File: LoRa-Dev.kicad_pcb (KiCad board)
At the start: 2 copper layers, 14 parts, among them J2 Barrel_Jack_MountingPin, U1 RPi Pico, U2 LT1963AEQ

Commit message: board layout
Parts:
- added C3: 47uF, Capacitor_SMD:CP_Elec_6.3x5.8, F.Cu at (126.5, 59.0)
- added C4: 0.1uF, Capacitor_SMD:C_0603_1608Metric, F.Cu at (128.0, 65.5)
- added J1: Conn_Coaxial_Small, Connector_Coaxial:U.FL_Hirose_U.FL-R-SMT-1_Vertical, F.Cu at (114.5, 60.0)
- added R9: R_Small, Resistor_SMD:R_0603_1608Metric, F.Cu at (126.7, 53.5)
- added U3: LoRa126XF30, LoRa-Dev:LoRa126XF30, F.Cu at (119.0, 82.5)
- moved U1 74.5 mm to (134.5, 41.1), turned to -90 degrees
- moved C1 2.50 mm to (143.0, 68.5)
- moved C2 2.00 mm to (152.0, 60.5)
- moved F1 2.00 mm to (159.0, 63.0)
- moved R7 2.00 mm to (156.0, 58.5)
- moved R8 2.00 mm to (159.0, 58.5)
- moved U2 2.00 mm to (138.6, 61.0)
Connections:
- net Net-(J2-Pad1) renamed /12V
- J2 pad MP: unconnected-(J2-MountPin-PadMP) -> GND
- U1 pad 26: unconnected-(U1-GP20-Pad26) -> /DIO3
- U1 pad 27: unconnected-(U1-GP21-Pad27) -> /DIO1
- U1 pad 29: unconnected-(U1-GP22-Pad29) -> /RESETn
- U1 pad 31: unconnected-(U1-GP26-Pad31) -> /BUSY
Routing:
- net /SPI_CSn: track 0.00 -> 60.4 mm, vias 0 -> 1
- net /SPI_SCK: track 0.00 -> 52.0 mm, vias 0 -> 1
- net RF_VDD: track 0.00 -> 49.8 mm, vias 0 -> 4
- net /BUSY: track 0.00 -> 45.5 mm, vias 0 -> 1
- net /DIO1: track 0.00 -> 45.4 mm, vias 0 -> 1
- net /SPI_MOSI: track 0.00 -> 44.7 mm, vias 0 -> 1
- net /SPI_MISO: track 0.00 -> 44.2 mm, vias 0 -> 1
- net /DIO3: track 0.00 -> 39.5 mm, vias 0 -> 1
- net /RESETn: track 0.00 -> 36.5 mm, vias 0 -> 1
- net /ANT: track 0.00 -> 10.0 mm
- net GND: track 21.3 -> 20.8 mm, vias 0 -> 32
- added copper zone on F.Cu, net /RF_GND
- added copper zone on In1.Cu, net /RF_GND
- added copper zone on B.Cu, net GND
- added copper zone on F.Cu, net GND
- added copper zone on In1.Cu, net GND
- added copper zone on In2.Cu, net GND
- added copper zone on F.Cu, net RF_VDD
- added copper zone on In2.Cu, net RF_VDD
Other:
- board outline added: 56 x 71 mm
- copper layers 2 -> 4

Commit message: Update silkscreen
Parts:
- R7: value 1k5 -> 4k7
- R8: value 4k7 -> 1k5
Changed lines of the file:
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@@
 		(tags "resistor")
 		(property "Reference" "R5"
-			(at 0 -2.62 0)
+			(at 4 0 90)
 			(layer "F.SilkS")
 			(effects
@@
 		(tags "resistor")
 		(property "Reference" "R8"
-			(at 0 -1.43 90)
+			(at 2.5 0 180)
 			(layer "F.SilkS")
 			(effects
@@
 			)
 		)
-		(property "Value" "4k7"
+		(property "Value" "1k5"
 			(at 0 1.43 90)
 			(layer "F.Fab")
@@
 		(tags "resistor")
 		(property "Reference" "R1"
-			(at 0 -2.62 90)
+			(at 0 -3 90)
 			(layer "F.SilkS")
 			(effects
@@
 		(tags "resistor")
 		(property "Reference" "R3"
-			(at 0 -2.62 0)
+			(at 4 0 90)
 			(layer "F.SilkS")
 			(effects
@@
 		(tags "resistor")
 		(property "Reference" "R4"
-			(at 0 -2.62 0)
+			(at 4 0 90)
 			(layer "F.SilkS")
 			(effects
@@
 		)
 		(fp_text user "${REFERENCE}"
-			(at 0.475 0 360)
+			(at 0.475 0 0)
 			(layer "F.Fab")
 			(effects
@@
 		(tags "fuse")
 		(property "Reference" "F1"
-			(at 0 -1.65 90)
+			(at 0 -2 90)
 			(layer "F.SilkS")
 			(effects
@@
 		(at 119 82.5 90)
 		(property "Reference" "U3"
-			(at 2 -0.5 90)
+			(at 17.5 -9 0)
 			(unlocked yes)
 			(layer "F.SilkS")
@@
 		(tags "capacitor")
 		(property "Reference" "C2"
-			(at -33.74 -28.65 90)
+			(at 4 0 180)
 			(layer "F.SilkS")
 			(effects
@@
 		(tags "capacitor")
 		(property "Reference" "C4"
-			(at 0 -1.43 0)
+			(at -3 0 0)
 			(layer "F.SilkS")
 			(effects
@@
 		(tags "capacitor")
 		(property "Reference" "C1"
-			(at 0 -4.3 0)
+			(at 0 3 0)
 			(layer "F.SilkS")
 			(effects
@@
 		(tags "resistor")
 		(property "Reference" "R6"
-			(at 12 -12.12 0)
+			(at 4 0 90)
 			(layer "F.SilkS")
 			(effects
@@
 		(tags "resistor")
 		(property "Reference" "R7"
-			(at 0 -1.43 90)
+			(at -2.5 0 180)
 			(layer "F.SilkS")
 			(effects
@@
 			)
 		)
-		(property "Value" "1k5"
+		(property "Value" "4k7"
 			(at 0 1.43 90)
 			(layer "F.Fab")
@@
 		(tags "resistor")
 		(property "Reference" "R9"
-			(at 0 -1.43 0)
+			(at -3.175 0 0)
 			(layer "F.SilkS")
 			(effects
@@
 		(tags "resistor")
 		(property "Reference" "R2"
-			(at 0 -2.62 90)
+			(at 0 -3 90)
 			(layer "F.SilkS")
 			(effects

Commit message: Added board id
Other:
- board text added: "LoRa126XF30 Dev Board 1.0"
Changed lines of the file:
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@@
 		(layer "Edge.Cuts")
+	)
+	(gr_text "LoRa126XF30\nDev Board 1.0"
+		(at 124 96.5 0)
+		(layer "B.SilkS")
+		(effects
+			(font
+				(size 1 1)
+				(thickness 0.1)
+			)
+			(justify left bottom mirror)
+		)
 	)
 	(segment

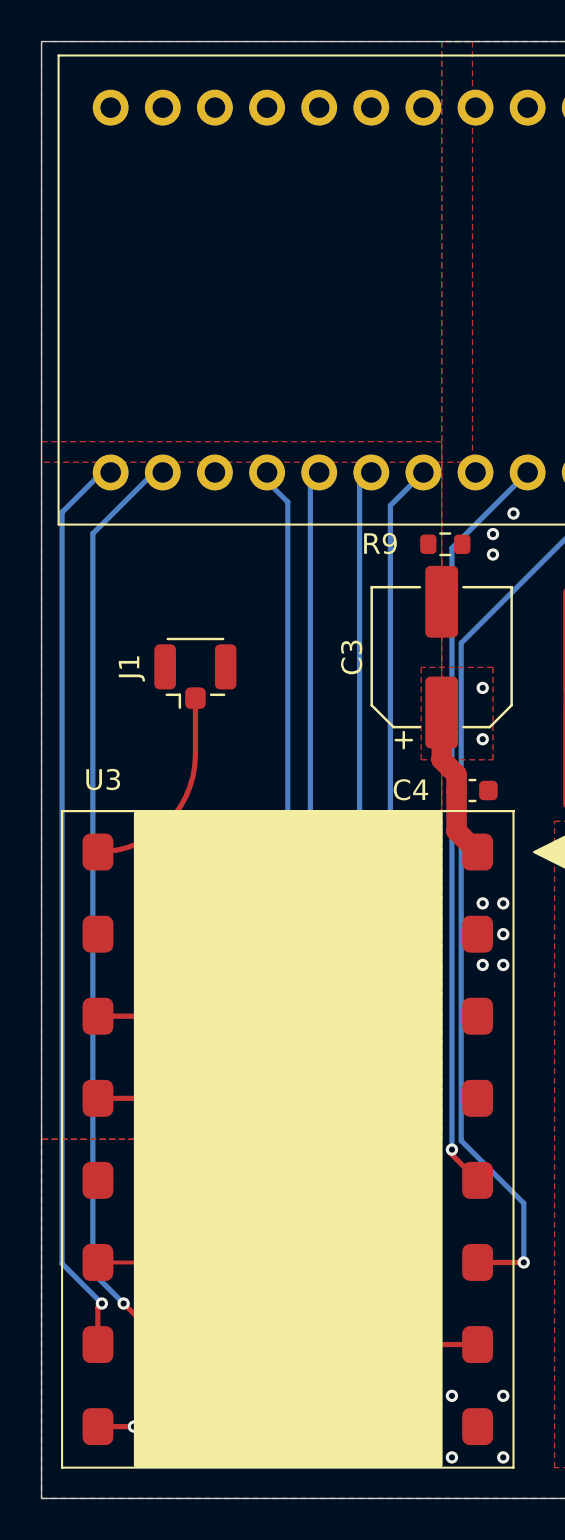
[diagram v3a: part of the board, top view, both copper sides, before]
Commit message: Updated RF GND
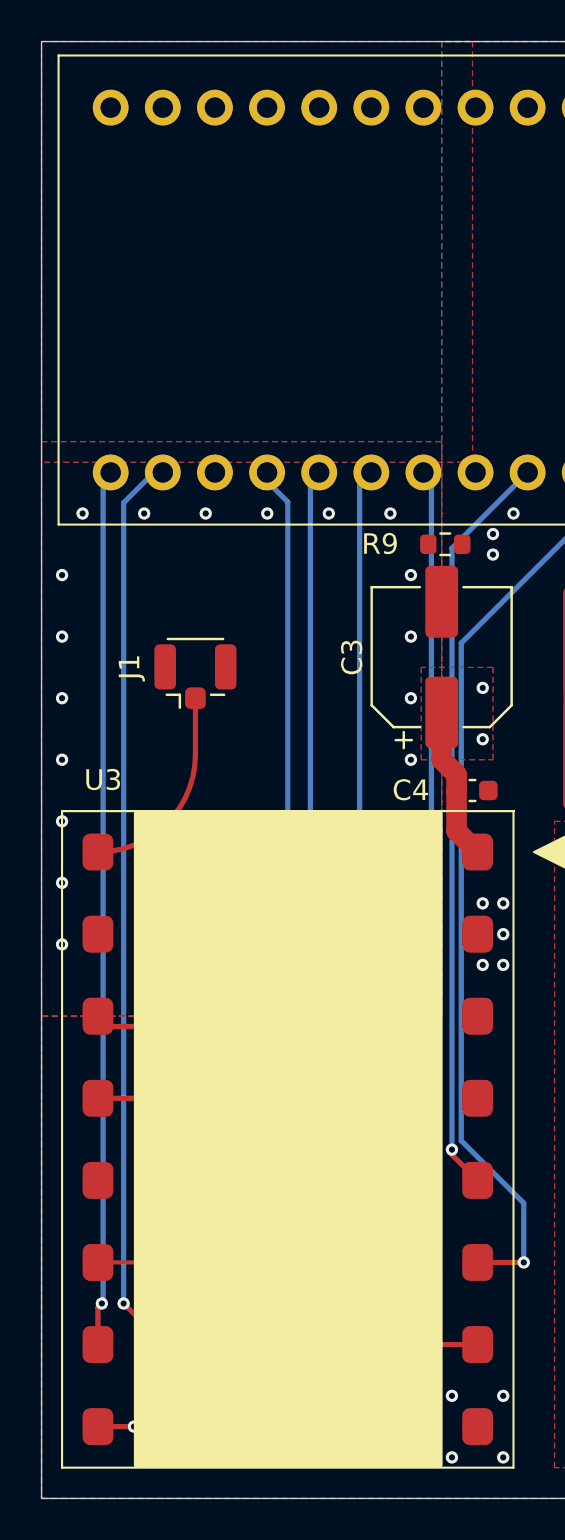
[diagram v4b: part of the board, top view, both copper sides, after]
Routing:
- net /SPI_MISO: track 44.2 -> 42.6 mm
- net /SPI_CSn: track 60.4 -> 59.2 mm
- net /RF_GND: vias 0 -> 25
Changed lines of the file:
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@@
 	)
 	(segment
-		(start 108 51.94)
+		(start 110 50.06)
 		(end 109.94 50)
 		(width 0.254)
@@
 	)
 	(segment
+		(start 110 90.44)
+		(end 110 50.06)
+		(width 0.254)
+		(layer "B.Cu")
+		(net 8)
+	)
+	(segment
 		(start 109.94 90.5)
-		(end 108 88.56)
-		(width 0.254)
-		(layer "B.Cu")
-		(net 8)
-	)
-	(segment
-		(start 108 88.56)
-		(end 108 51.94)
+		(end 110 90.44)
 		(width 0.254)
 		(layer "B.Cu")
@@
 	)
 	(segment
-		(start 109.5 89)
-		(end 109.5 52.98)
+		(start 111 90.5)
+		(end 111 51.48)
 		(width 0.254)
 		(layer "B.Cu")
@@
 	)
 	(segment
-		(start 111 90.5)
-		(end 109.5 89)
-		(width 0.254)
-		(layer "B.Cu")
-		(net 18)
-	)
-	(segment
-		(start 109.5 52.98)
+		(start 111 51.48)
 		(end 112.48 50)
 		(width 0.254)
@@
 	(segment
 		(start 124 80.5)
-		(end 124 51.61)
+		(end 126 78.5)
 		(width 0.254)
 		(layer "B.Cu")
@@
 	)
 	(segment
-		(start 124 51.61)
+		(start 126 78.5)
+		(end 126 50.39)
+		(width 0.254)
+		(layer "B.Cu")
+		(net 35)
+	)
+	(segment
+		(start 126 50.39)
 		(end 125.61 50)
 		(width 0.254)
@@
 	)
 	(segment
+		(start 110.25 77)
+		(end 122 77)
+		(width 0.254)
+		(layer "F.Cu")
+		(net 37)
+	)
+	(segment
 		(start 109.75 76.5)
+		(end 110.25 77)
+		(width 0.254)
+		(layer "F.Cu")
+		(net 37)
+	)
+	(segment
+		(start 122 77)
 		(end 122.5 76.5)
 		(width 0.254)
@@
 		(layer "F.Cu")
 		(net 40)
+	)
+	(via
+		(at 108 61)
+		(size 0.6)
+		(drill 0.3)
+		(layers "F.Cu" "B.Cu")
+		(free yes)
+		(net 41)
+	)
+	(via
+		(at 121 52)
+		(size 0.6)
+		(drill 0.3)
+		(layers "F.Cu" "B.Cu")
+		(free yes)
+		(net 41)
+	)
+	(via
+		(at 112 52)
+		(size 0.6)
+		(drill 0.3)
+		(layers "F.Cu" "B.Cu")
+		(free yes)
+		(net 41)
+	)
+	(via
+		(at 125 55)
+		(size 0.6)
+		(drill 0.3)
+		(layers "F.Cu" "B.Cu")
+		(free yes)
+		(net 41)
+	)
+	(via
+		(at 112 76)
+		(size 0.6)
+		(drill 0.3)
+		(layers "F.Cu" "B.Cu")
+		(free yes)
+		(net 41)
+	)
+	(via
+		(at 115 52)
+		(size 0.6)
+		(drill 0.3)
+		(layers "F.Cu" "B.Cu")
+		(free yes)
+		(net 41)
+	)
+	(via
+		(at 118 52)
+		(size 0.6)
+		(drill 0.3)
+		(layers "F.Cu" "B.Cu")
+		(free yes)
+		(net 41)
+	)
+	(via
+		(at 125 73)
+		(size 0.6)
+		(drill 0.3)
+		(layers "F.Cu" "B.Cu")
+		(free yes)
+		(net 41)
+	)
+	(via
+		(at 115 76)
+		(size 0.6)
+		(drill 0.3)
+		(layers "F.Cu" "B.Cu")
+		(free yes)
+		(net 41)
+	)
+	(via
+		(at 124 76)
+		(size 0.6)
+		(drill 0.3)
+		(layers "F.Cu" "B.Cu")
+		(free yes)
+		(net 41)
+	)
+	(via
+		(at 108 55)
+		(size 0.6)
+		(drill 0.3)
+		(layers "F.Cu" "B.Cu")
+		(free yes)
+		(net 41)
+	)
+	(via
+		(at 125 58)
+		(size 0.6)
+		(drill 0.3)
+		(layers "F.Cu" "B.Cu")
+		(free yes)
+		(net 41)
+	)
+	(via
+		(at 124 52)
+		(size 0.6)
+		(drill 0.3)
+		(layers "F.Cu" "B.Cu")
+		(free yes)
+		(net 41)
+	)
+	(via
+		(at 125 61)
+		(size 0.6)
+		(drill 0.3)
+		(layers "F.Cu" "B.Cu")
+		(free yes)
+		(net 41)
+	)
+	(via
+		(at 109 52)
+		(size 0.6)
+		(drill 0.3)
+		(layers "F.Cu" "B.Cu")
+		(free yes)
+		(net 41)
+	)
+	(via
+		(at 125 67)
+		(size 0.6)
+		(drill 0.3)
+		(layers "F.Cu" "B.Cu")
+		(free yes)
+		(net 41)
+	)
+	(via
+		(at 108 73)
+		(size 0.6)
+		(drill 0.3)
+		(layers "F.Cu" "B.Cu")
+		(free yes)
+		(net 41)
+	)
+	(via
+		(at 125 70)
+		(size 0.6)
+		(drill 0.3)
+		(layers "F.Cu" "B.Cu")
+		(free yes)
+		(net 41)
+	)
+	(via
+		(at 121 76)
+		(size 0.6)
+		(drill 0.3)
+		(layers "F.Cu" "B.Cu")
+		(free yes)
+		(net 41)
+	)
+	(via
+		(at 108 67)
+		(size 0.6)
+		(drill 0.3)
+		(layers "F.Cu" "B.Cu")
+		(free yes)
+		(net 41)
+	)
+	(via
+		(at 108 70)
+		(size 0.6)
+		(drill 0.3)
+		(layers "F.Cu" "B.Cu")
+		(free yes)
+		(net 41)
+	)
+	(via
+		(at 125 64)
+		(size 0.6)
+		(drill 0.3)
+		(layers "F.Cu" "B.Cu")
+		(free yes)
+		(net 41)
+	)
+	(via
+		(at 118 76)
+		(size 0.6)
+		(drill 0.3)
+		(layers "F.Cu" "B.Cu")
+		(free yes)
+		(net 41)
+	)
+	(via
+		(at 108 64)
+		(size 0.6)
+		(drill 0.3)
+		(layers "F.Cu" "B.Cu")
+		(free yes)
+		(net 41)
+	)
+	(via
+		(at 108 58)
+		(size 0.6)
+		(drill 0.3)
+		(layers "F.Cu" "B.Cu")
+		(free yes)
+		(net 41)
 	)
 	(zone
@@
 		(polygon
 			(pts
-				(xy 107 48.5) (xy 126.5 48.5) (xy 126.5 82.5) (xy 107 82.5)
+				(xy 107 48.5) (xy 126.5 48.5) (xy 126.5 76.5) (xy 107 76.5)
 			)
 		)
@@
 		(polygon
 			(pts
-				(xy 126.5 29) (xy 126.5 82.5) (xy 107 82.5) (xy 107 100) (xy 163 100) (xy 163 29)
+				(xy 126.5 29) (xy 126.5 76.5) (xy 107 76.5) (xy 107 100) (xy 163 100) (xy 163 29)
 			)
 		)

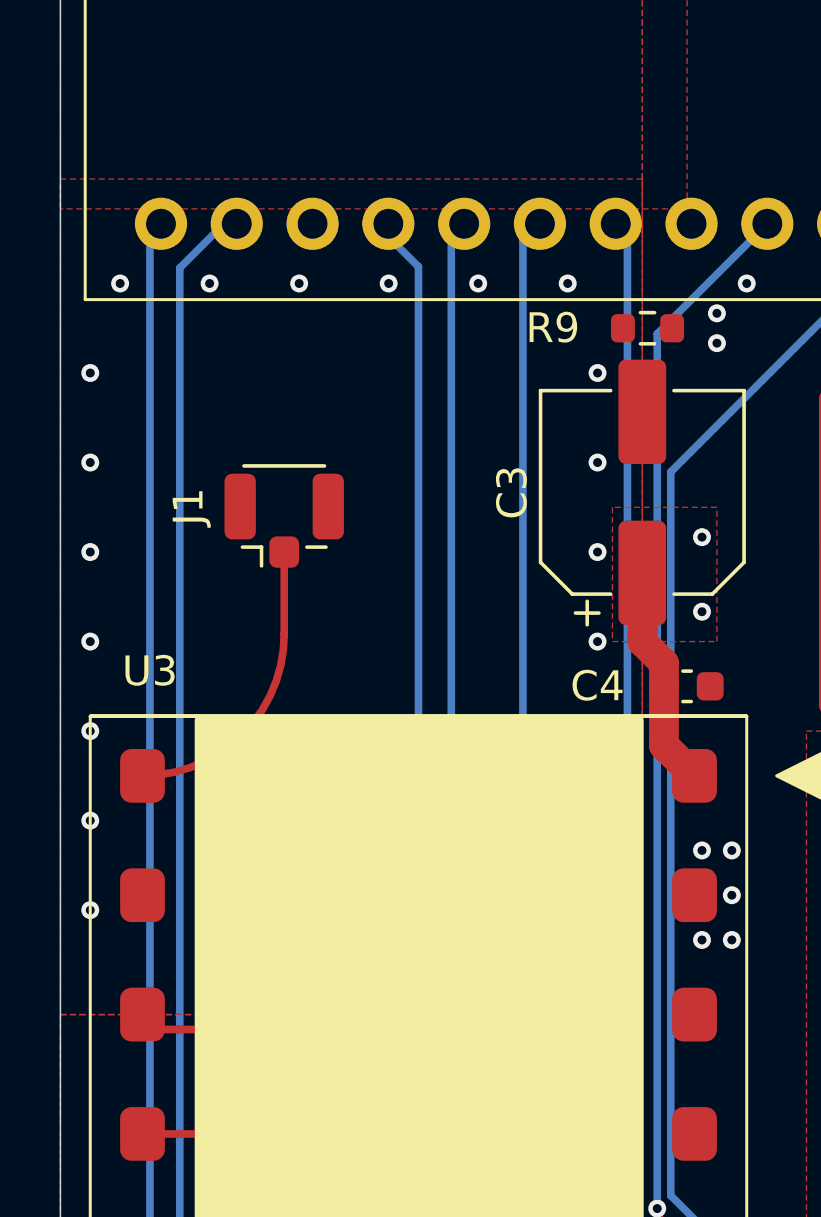
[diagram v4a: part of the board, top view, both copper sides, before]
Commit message: Actually fixed RF GND
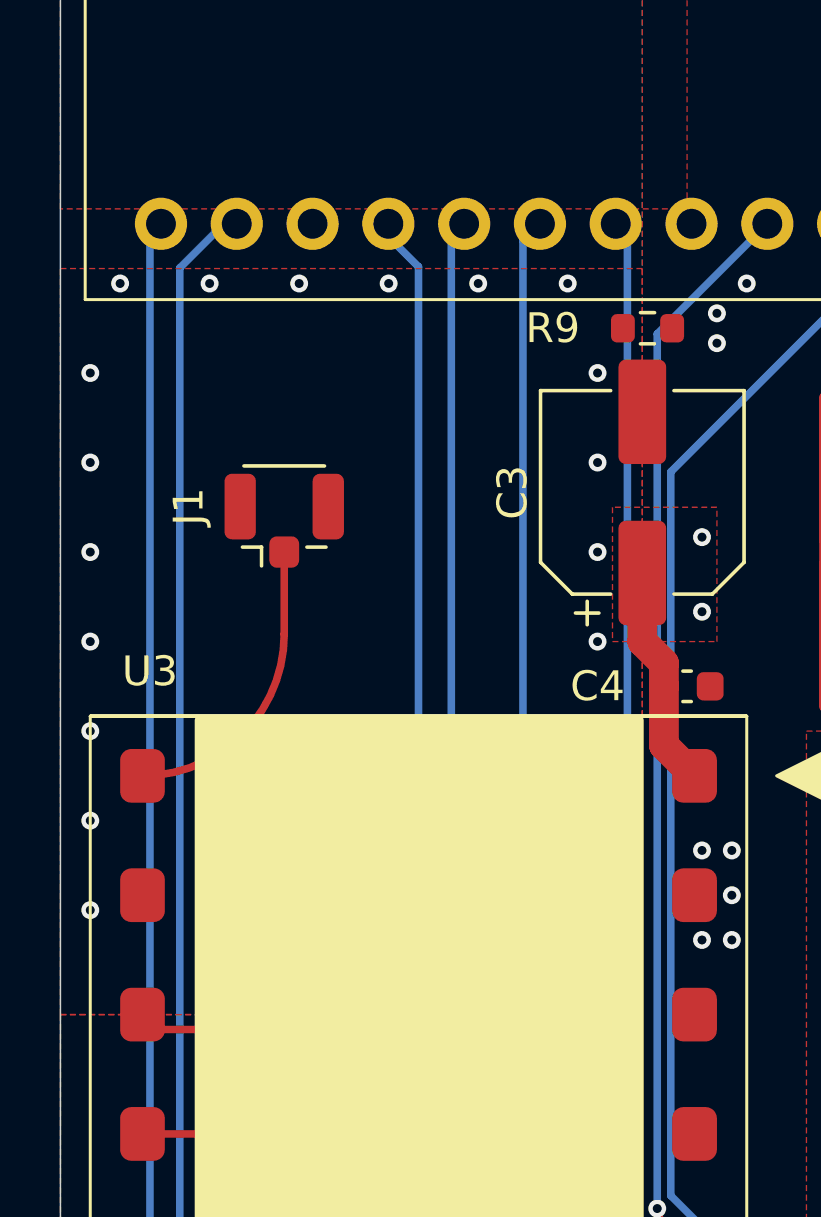
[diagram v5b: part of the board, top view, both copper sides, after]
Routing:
- net RF_VDD: track 49.8 -> 52.3 mm
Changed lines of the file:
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@@
+	)
+	(segment
+		(start 128.5 60.5)
+		(end 128.5 63)
+		(width 2)
+		(layer "In2.Cu")
+		(net 4)
 	)
 	(segment
@@
 	(segment
 		(start 110.25 77)
-		(end 122 77)
+		(end 109.75 76.5)
 		(width 0.254)
 		(layer "F.Cu")
@@
 	)
 	(segment
-		(start 109.75 76.5)
+		(start 122 77)
 		(end 110.25 77)
 		(width 0.254)
 		(layer "F.Cu")
+		(net 37)
+	)
+	(via
+		(at 122 77)
+		(size 0.6)
+		(drill 0.3)
+		(layers "F.Cu" "B.Cu")
+		(net 37)
+	)
+	(segment
+		(start 122.5 76.5)
+		(end 122.5 50.57)
+		(width 0.254)
+		(layer "B.Cu")
 		(net 37)
 	)
@@
 		(end 122.5 76.5)
 		(width 0.254)
-		(layer "F.Cu")
-		(net 37)
-	)
-	(via
-		(at 122.5 76.5)
-		(size 0.6)
-		(drill 0.3)
-		(layers "F.Cu" "B.Cu")
+		(layer "B.Cu")
 		(net 37)
 	)
@@
 		(start 122.5 50.57)
 		(end 123.07 50)
-		(width 0.254)
-		(layer "B.Cu")
-		(net 37)
-	)
-	(segment
-		(start 122.5 76.5)
-		(end 122.5 50.57)
 		(width 0.254)
 		(layer "B.Cu")
@@
 		(polygon
 			(pts
-				(xy 107 48.5) (xy 126.5 48.5) (xy 126.5 76.5) (xy 107 76.5)
+				(xy 107 51.5) (xy 126.5 51.5) (xy 126.5 76.5) (xy 107 76.5)
 			)
 		)
